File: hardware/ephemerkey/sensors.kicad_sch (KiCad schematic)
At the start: 0 parts

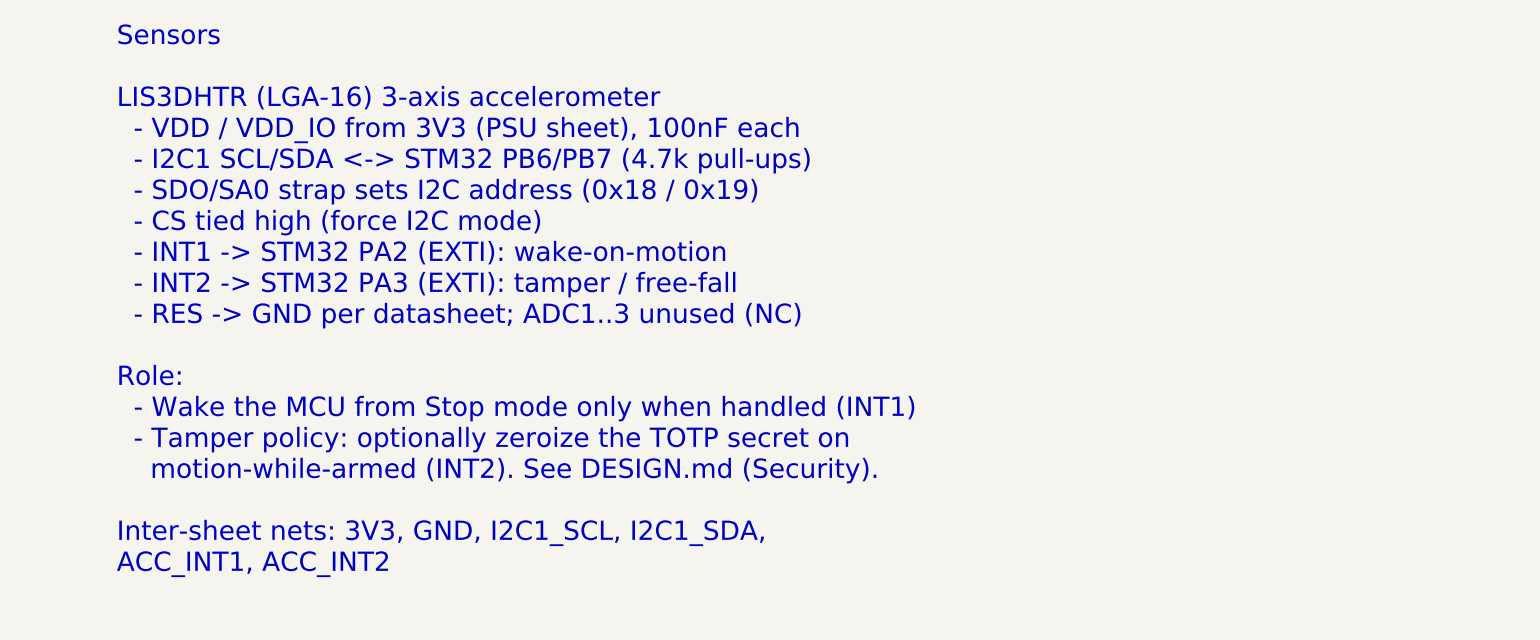
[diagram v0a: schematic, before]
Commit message: Populate schematic sheets per subsystem (placed, not wired)
Adopt the house schgen workflow (kschgen.py + manifest), matching notchdeck/
tsumikoro: schematic is GENERATED from scripts/ephemerkey.schgen.py, parts
PLACED with per-sheet on-canvas wiring notes; wiring is the next eeschema phase.

57 components across MCU / PSU / GNSS / Sensors, every line on a real KiCad
bundled symbol+footprint and a JLCPCB LCSC (0402 passives, 0805 bulk):
- MCU: STM32U083KCU6, 32.768kHz LSE crystal (C32346) + 12pF loads, SWD TC2030,
  lock-out header, decoupling, BOOT0/NRST, button, status LEDs.
- PSU: USB-C (GCT USB4105) + USBLC6 ESD + 5.1k CC, MCP73831 charger (Rprog 4.7k
  ~213mA for 500mAh), AO3401A load-share + B5819W, TPS63900 + FNR3015 2.2µH
  (small) + 10µF caps, JST-PH RA battery (S2B-PH-K-S).
- GNSS: MAX-M10S + W3011A + pi-match (series 0R, shunts DNP), VCC_RF ferrite,
  V_BCKP/V_IO/VCC decoupling.
- Sensors: LIS3DH + decoupling + 4.7k I2C pull-ups.

Tooling: kschgen.py, kicad-sch-check.py, kicad-sch-render.sh; Makefile gen/
check/render targets. make check: 57 comps, 57/57 footprints, no dup refs.
Added hardware/PARTS.md (BOM source of truth). CLAUDE.md documents the workflow.

Co-Authored-By: Claude Opus 4.8 (1M context) <noreply@anthropic.com>
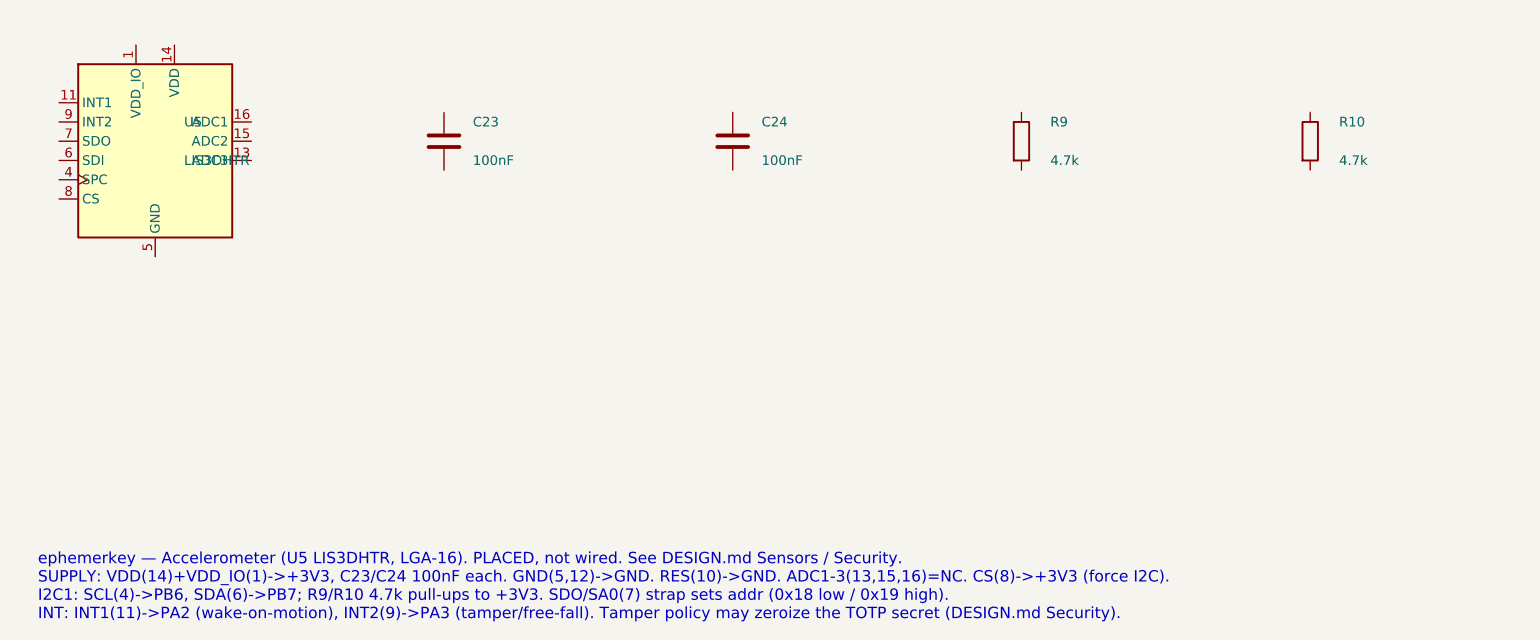
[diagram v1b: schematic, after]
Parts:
- added C23, C24: 100nF, Capacitor_SMD:C_0402_1005Metric, symbol Device:C
- added R10, R9: 4.7k, Resistor_SMD:R_0402_1005Metric, symbol Device:R
- added U5: LIS3DHTR, Package_LGA:LGA-16_3x3mm_P0.5mm, symbol Sensor_Motion:LIS3DH
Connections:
- new net: U5.10 (GND), U5.12 (GND), U5.5 (GND)
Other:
- note added: "ephemerkey — Accelerometer (U5 LIS3DHTR, LGA-16). PLACED, not wired. See DESIGN.md Sensors / Security. SUPPLY: VDD(14)+VDD_IO(1)->+3V3, C23/C24 100nF each. GND(5,12)->GND. RES(10)->GND. ADC1-3(13,15,16)=NC. CS(8)->+3V3 (force I2C). I2C1: SCL(4)->PB6, SDA(6)->PB7; R9/R10 4.7k pull-ups to +3V3. SDO/SA0(7) strap sets addr (0x18 low / 0x19 high). INT: INT1(11)->PA2 (wake-on-motion), INT2(9)->PA3 (tam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"
- note removed: "Sensors LIS3DHTR (LGA-16) 3-axis accelerometer - VDD / VDD_IO from 3V3 (PSU sheet), 100nF each - I2C1 SCL/SDA <-> STM32 PB6/PB7 (4.7k pull-ups) - SDO/SA0 strap sets I2C address (0x18 / 0x19) - CS tied high (force I2C mode) - INT1 -> STM32 PA2 (EXTI): wake-on-motion - INT2 -> STM32 PA3 (EXTI): tamper / free-fall - RES -> GND per datasheet; ADC1..3 unused (NC) Role: - Wake the MCU from Stop mode on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"
- company: (none) -> EphemerKey Authors
- title: ephemerkey — Sensors -> ephemerkey — Accelerometer (LIS3DH)
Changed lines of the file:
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@@
 	(paper "A3")
 	(title_block
-		(title "ephemerkey — Sensors")
+		(title "ephemerkey — Accelerometer (LIS3DH)")
 		(date "2026-06-21")
 		(rev "0.1")
-		(comment 1 "LIS3DH 3-axis accelerometer")
-		(comment 2 "Motion wake + tamper detection")
-	)
-	(text "Sensors\n\nLIS3DHTR (LGA-16) 3-axis accelerometer\n  - VDD / VDD_IO from 3V3 (PSU sheet), 100nF each\n  - I2C1 SCL/SDA <-> STM32 PB6/PB7 (4.7k pull-ups)\n  - SDO/SA0 strap sets I2C address (0x18 / 0x19)\n  - CS tied high (force I2C mode)\n  - INT1 -> STM32 PA2 (EXTI): wake-on-motion\n  - INT2 -> STM32 PA3 (EXTI): tamper / free-fall\n  - RES -> GND per datasheet; ADC1..3 unused (NC)\n\nRole:\n  - Wake the MCU from Stop mode only when handled (INT1)\n  - Tamper policy: optionally zeroize the TOTP secret on\n    motion-while-armed (INT2). See DESIGN.md (Security).\n\nInter-sheet nets: 3V3, GND, I2C1_SCL, I2C1_SDA,\nACC_INT1, ACC_INT2"
-		(exclude_from_sim no)
-		(at 25.4 25.4 0)
-		(effects
-			(font
-				(size 2.54 2.54)
-			)
-			(justify left top)
-		)
+		(company "EphemerKey Authors")
+	)
+	(symbol
+		(lib_id "Sensor_Motion:LIS3DH")
+		(at 30.4800 40.6400 0)
+		(unit 1)
+		(exclude_from_sim no)
+		(in_bom yes)
+		(on_board yes)
+		(dnp no)
+		(property "Reference" "U5"
+			(at 34.2900 38.1000 0)
+			(effects (font (size 1.27 1.27)) (justify left))
+		)
+		(property "Value" "LIS3DHTR"
+			(at 34.2900 43.1800 0)
+			(effects (font (size 1.27 1.27)) (justify left))
+		)
+		(property "Footprint" "Package_LGA:LGA-16_3x3mm_P0.5mm"
+			(at 30.4800 40.6400 0)
+			(effects (font (size 1.27 1.27))) (hide yes)
+		)
+		(property "Datasheet" "~"
+			(at 30.4800 40.6400 0)
+			(effects (font (size 1.27 1.27))) (hide yes)
+		)
+		(property "LCSC" "C15134"
+			(at 30.4800 40.6400 0)
+			(effects (font (size 1.27 1.27))) (hide yes)
+		)
+		(property "MPN" "LIS3DHTR"
+			(at 30.4800 40.6400 0)
+			(effects (font (size 1.27 1.27))) (hide yes)
+		)
+		(property "Manufacturer" "STMicroelectronics"
+			(at 30.4800 40.6400 0)
+			(effects (font (size 1.27 1.27))) (hide yes)
+		)
+		(pin "1")
+		(pin "2")
+		(pin "3")
+		(pin "4")
+		(pin "5")
+		(pin "6")
+		(pin "7")
+		(pin "8")
+		(pin "9")
+		(pin "10")
+		(pin "11")
+		(pin "12")
+		(pin "13")
+		(pin "14")
+		(pin "15")
+		(pin "16")
+		(instances
+			(project "ephemerkey"
+				(path "/e1000000-0000-4000-8000-000000000001/1e926eec-7edd-43b0-8208-0483c976793a"
+					(reference "U5")
+					(unit 1)
+				)
+			)
+		)
+	)
+	(symbol
+		(lib_id "Device:C")
+		(at 68.5800 40.6400 0)
+		(unit 1)
+		(exclude_from_sim no)
+		(in_bom yes)
+		(on_board yes)
+		(dnp no)
+		(property "Reference" "C23"
+			(at 72.3900 38.1000 0)
+			(effects (font (size 1.27 1.27)) (justify left))
+		)
+		(property "Value" "100nF"
+			(at 72.3900 43.1800 0)
+			(effects (font (size 1.27 1.27)) (justify left))
+		)
+		(property "Footprint" "Capacitor_SMD:C_0402_1005Metric"
+			(at 68.5800 40.6400 0)
+			(effects (font (size 1.27 1.27))) (hide yes)
+		)
+		(property "Datasheet" "~"
+			(at 68.5800 40.6400 0)
+			(effects (font (size 1.27 1.27))) (hide yes)
+		)
+		(property "LCSC" "C1525"
+			(at 68.5800 40.6400 0)
+			(effects (font (size 1.27 1.27))) (hide yes)
+		)
+		(pin "1")
+		(pin "2")
+		(instances
+			(project "ephemerkey"
+				(path "/e1000000-0000-4000-8000-000000000001/1e926eec-7edd-43b0-8208-0483c976793a"
+					(reference "C23")
+					(unit 1)
+				)
+			)
+		)
+	)
+	(symbol
+		(lib_id "Device:C")
+		(at 106.6800 40.6400 0)
+		(unit 1)
+		(exclude_from_sim no)
+		(in_bom yes)
+		(on_board yes)
+		(dnp no)
+		(property "Reference" "C24"
+			(at 110.4900 38.1000 0)
+			(effects (font (size 1.27 1.27)) (justify left))
+		)
+		(property "Value" "100nF"
+			(at 110.4900 43.1800 0)
+			(effects (font (size 1.27 1.27)) (justify left))
+		)
+		(property "Footprint" "Capacitor_SMD:C_0402_1005Metric"
+			(at 106.6800 40.6400 0)
+			(effects (font (size 1.27 1.27))) (hide yes)
+		)
+		(property "Datasheet" "~"
+			(at 106.6800 40.6400 0)
+			(effects (font (size 1.27 1.27))) (hide yes)
+		)
+		(property "LCSC" "C1525"
+			(at 106.6800 40.6400 0)
+			(effects (font (size 1.27 1.27))) (hide yes)
+		)
+		(pin "1")
+		(pin "2")
+		(instances
+			(project "ephemerkey"
+				(path "/e1000000-0000-4000-8000-000000000001/1e926eec-7edd-43b0-8208-0483c976793a"
+					(reference "C24")
+					(unit 1)
+				)
+			)
+		)
+	)
+	(symbol
+		(lib_id "Device:R")
+		(at 144.7800 40.6400 0)
+		(unit 1)
+		(exclude_from_sim no)
+		(in_bom yes)
+		(on_board yes)
+		(dnp no)
+		(property "Reference" "R9"
+			(at 148.5900 38.1000 0)
+			(effects (font (size 1.27 1.27)) (justify left))
+		)
+		(property "Value" "4.7k"
+			(at 148.5900 43.1800 0)
+			(effects (font (size 1.27 1.27)) (justify left))
+		)
+		(property "Footprint" "Resistor_SMD:R_0402_1005Metric"
+			(at 144.7800 40.6400 0)
+			(effects (font (size 1.27 1.27))) (hide yes)
+		)
+		(property "Datasheet" "~"
+			(at 144.7800 40.6400 0)
+			(effects (font (size 1.27 1.27))) (hide yes)
+		)
+		(property "LCSC" "C25900"
+			(at 144.7800 40.6400 0)
+			(effects (font (size 1.27 1.27))) (hide yes)
+		)
+		(pin "1")
+		(pin "2")
+		(instances
+			(project "ephemerkey"
+				(path "/e1000000-0000-4000-8000-000000000001/1e926eec-7edd-43b0-8208-0483c976793a"
+					(reference "R9")
+					(unit 1)
+				)
+			)
+		)
+	)
+	(symbol
+		(lib_id "Device:R")
+		(at 182.8800 40.6400 0)
+		(unit 1)
+		(exclude_from_sim no)
+		(in_bom yes)
+		(on_board yes)
+		(dnp no)
+		(property "Reference" "R10"
+			(at 186.6900 38.1000 0)
+			(effects (font (size 1.27 1.27)) (justify left))
+		)
+		(property "Value" "4.7k"
+			(at 186.6900 43.1800 0)
+			(effects (font (size 1.27 1.27)) (justify left))
+		)
+		(property "Footprint" "Resistor_SMD:R_0402_1005Metric"
+			(at 182.8800 40.6400 0)
+			(effects (font (size 1.27 1.27))) (hide yes)
+		)
+		(property "Datasheet" "~"
+			(at 182.8800 40.6400 0)
+			(effects (font (size 1.27 1.27))) (hide yes)
+		)
+		(property "LCSC" "C25900"
+			(at 182.8800 40.6400 0)
+			(effects (font (size 1.27 1.27))) (hide yes)
+		)
+		(pin "1")
+		(pin "2")
+		(instances
+			(project "ephemerkey"
+				(path "/e1000000-0000-4000-8000-000000000001/1e926eec-7edd-43b0-8208-0483c976793a"
+					(reference "R10")
+					(unit 1)
+				)
+			)
+		)
+	)
+	(text "ephemerkey — Accelerometer (U5 LIS3DHTR, LGA-16). PLACED, not wired. See DESIGN.md Sensors / Security.\nSUPPLY: VDD(14)+VDD_IO(1)->+3V3, C23/C24 100nF each. GND(5,12)->GND. RES(10)->GND. ADC1-3(13,15,16)=NC. CS(8)->+3V3 (force I2C).\nI2C1: SCL(4)->PB6, SDA(6)->PB7; R9/R10 4.7k pull-ups to +3V3. SDO/SA0(7) strap sets addr (0x18 low / 0x19 high).\nINT: INT1(11)->PA2 (wake-on-motion), INT2(9)->PA3 (tamper/free-fall). Tamper policy may zeroize the TOTP secret (DESIGN.md Security)."
+		(exclude_from_sim no)
+		(at 15.00 95.00 0)
+		(effects (font (size 1.5 1.5)) (justify left top))
 	)
 	(sheet_instances
-		(path "/e4000000-0000-4000-8000-000000000004"
-			(page "4")
-		)
-	)
+		(path "/"
+			(page "5")
+		)
+	)

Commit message: Pinout-guide notes; vendor MAX + switch 3D models; 3 user buttons + DFU
Wiring notes: rewrote the four sheet notes from run-on prose into per-pin
PINOUT GUIDES (pin → net/function tables) per request.

3D models:
- MAX-M10S: vendored ublox_MAX-M10S.step (u-blox MAX form-factor, AP214, from
  fcmadwar/3D-Step-Models-Library) + project footprint ephemerkey:ublox_MAX
  with (model) repointed. Verify offset/rotation in 3D viewer.
- Switches: reuse tsumikoro's vendored ephemerkey:SW_Push_1P1T_XKB_TS-1187A
  footprint + STEP (the XKB TS-1187A model isn't in this KiCad bundle).
- Remaining to download: STM32U083 (UFQFPN-32), W3011A.

Switches: 3 user buttons (SW1→PA5, SW2→PA15 active-low; SW3→PF3/BOOT0
active-high). Holding SW3 at reset enters the STM32U0 ROM bootloader → USB DFU
over USB-C (confirmed in AN2606; crystal-less USB via HSI48+CRS).

make check: 59 components, 59/59 footprints, no dup refs. DESIGN.md pin budget +
library map, PARTS.md, 3dmodels README updated.

Co-Authored-By: Claude Opus 4.8 (1M context) <noreply@anthropic.com>
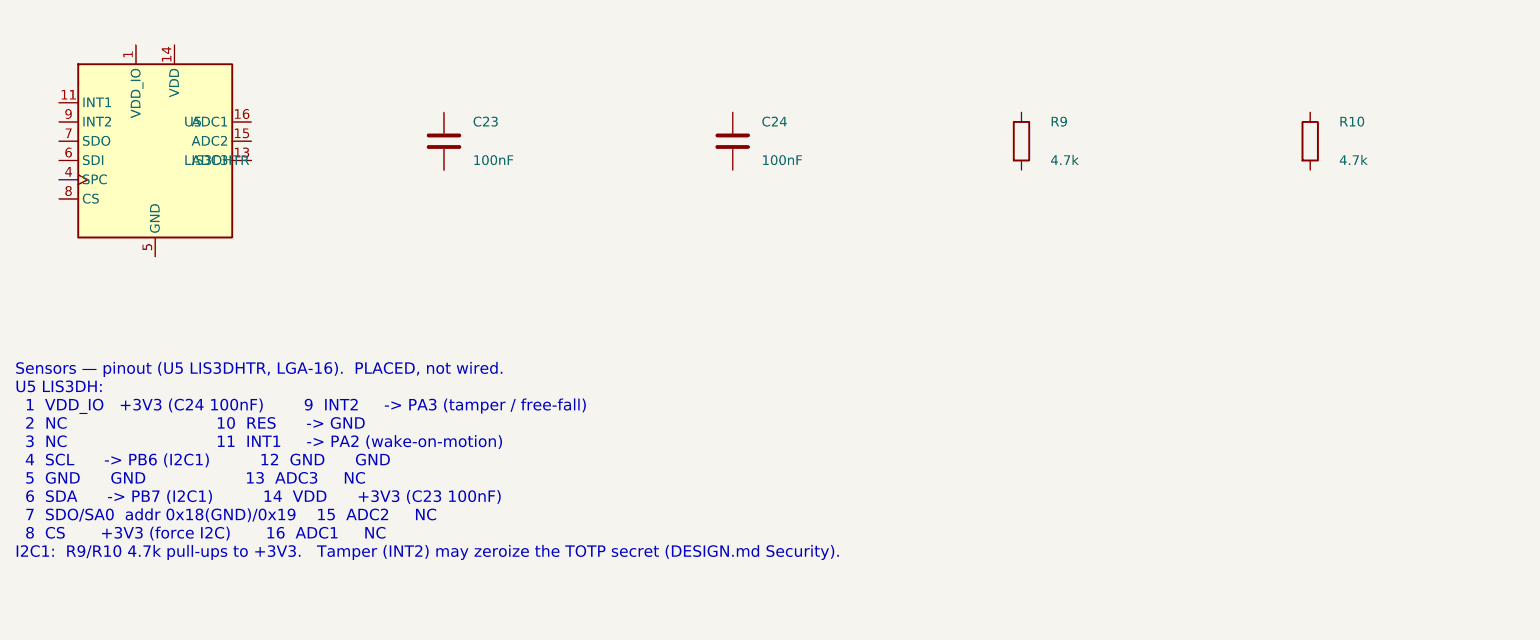
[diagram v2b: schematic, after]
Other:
- note added: "Sensors — pinout (U5 LIS3DHTR, LGA-16). PLACED, not wired. U5 LIS3DH: 1 VDD_IO +3V3 (C24 100nF) 9 INT2 -> PA3 (tamper / free-fall) 2 NC 10 RES -> GND 3 NC 11 INT1 -> PA2 (wake-on-motion) 4 SCL -> PB6 (I2C1) 12 GND GND 5 GND GND 13 ADC3 NC 6 SDA -> PB7 (I2C1) 14 VDD +3V3 (C23 100nF) 7 SDO/SA0 addr 0x18(GND)/0x19 15 ADC2 NC 8 CS +3V3 (force I2C) 16 ADC1 NC I2C1: R9/R10 4.7k pull-ups to +3V3. Tamper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"
- note removed: "ephemerkey — Accelerometer (U5 LIS3DHTR, LGA-16). PLACED, not wired. See DESIGN.md Sensors / Security. SUPPLY: VDD(14)+VDD_IO(1)->+3V3, C23/C24 100nF each. GND(5,12)->GND. RES(10)->GND. ADC1-3(13,15,16)=NC. CS(8)->+3V3 (force I2C). I2C1: SCL(4)->PB6, SDA(6)->PB7; R9/R10 4.7k pull-ups to +3V3. SDO/SA0(7) strap sets addr (0x18 low / 0x19 high). INT: INT1(11)->PA2 (wake-on-motion), INT2(9)->PA3 (tam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"
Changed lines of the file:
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@@
 		(instances
 			(project "ephemerkey"
-				(path "/e1000000-0000-4000-8000-000000000001/1e926eec-7edd-43b0-8208-0483c976793a"
+				(path "/e1000000-0000-4000-8000-000000000001/839db5ae-e5cf-439c-84ec-b2fb949c31ee"
 					(reference "U5")
 					(unit 1)
@@
 		(instances
 			(project "ephemerkey"
-				(path "/e1000000-0000-4000-8000-000000000001/1e926eec-7edd-43b0-8208-0483c976793a"
+				(path "/e1000000-0000-4000-8000-000000000001/839db5ae-e5cf-439c-84ec-b2fb949c31ee"
 					(reference "C23")
 					(unit 1)
@@
 		(instances
 			(project "ephemerkey"
-				(path "/e1000000-0000-4000-8000-000000000001/1e926eec-7edd-43b0-8208-0483c976793a"
+				(path "/e1000000-0000-4000-8000-000000000001/839db5ae-e5cf-439c-84ec-b2fb949c31ee"
 					(reference "C24")
 					(unit 1)
@@
 		(instances
 			(project "ephemerkey"
-				(path "/e1000000-0000-4000-8000-000000000001/1e926eec-7edd-43b0-8208-0483c976793a"
+				(path "/e1000000-0000-4000-8000-000000000001/839db5ae-e5cf-439c-84ec-b2fb949c31ee"
 					(reference "R9")
 					(unit 1)
@@
 		(instances
 			(project "ephemerkey"
-				(path "/e1000000-0000-4000-8000-000000000001/1e926eec-7edd-43b0-8208-0483c976793a"
+				(path "/e1000000-0000-4000-8000-000000000001/839db5ae-e5cf-439c-84ec-b2fb949c31ee"
 					(reference "R10")
 					(unit 1)
@@
 		)
 	)
-	(text "ephemerkey — Accelerometer (U5 LIS3DHTR, LGA-16). PLACED, not wired. See DESIGN.md Sensors / Security.\nSUPPLY: VDD(14)+VDD_IO(1)->+3V3, C23/C24 100nF each. GND(5,12)->GND. RES(10)->GND. ADC1-3(13,15,16)=NC. CS(8)->+3V3 (force I2C).\nI2C1: SCL(4)->PB6, SDA(6)->PB7; R9/R10 4.7k pull-ups to +3V3. SDO/SA0(7) strap sets addr (0x18 low / 0x19 high).\nINT: INT1(11)->PA2 (wake-on-motion), INT2(9)->PA3 (tamper/free-fall). Tamper policy may zeroize the TOTP secret (DESIGN.md Security)."
+	(text "Sensors — pinout (U5 LIS3DHTR, LGA-16).  PLACED, not wired.\nU5 LIS3DH:\n  1  VDD_IO   +3V3 (C24 100nF)        9  INT2     -> PA3 (tamper / free-fall)\n  2  NC                              10  RES      -> GND\n  3  NC                              11  INT1     -> PA2 (wake-on-motion)\n  4  SCL      -> PB6 (I2C1)          12  GND      GND\n  5  GND      GND                    13  ADC3     NC\n  6  SDA      -> PB7 (I2C1)          14  VDD      +3V3 (C23 100nF)\n  7  SDO/SA0  addr 0x18(GND)/0x19    15  ADC2     NC\n  8  CS       +3V3 (force I2C)       16  ADC1     NC\nI2C1:  R9/R10 4.7k pull-ups to +3V3.   Tamper (INT2) may zeroize the TOTP secret (DESIGN.md Security)."
 		(exclude_from_sim no)
-		(at 15.00 95.00 0)
+		(at 12.00 70.00 0)
 		(effects (font (size 1.5 1.5)) (justify left top))
 	)
